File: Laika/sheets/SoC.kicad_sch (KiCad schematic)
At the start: 2 parts, among them J6 Conn_01x03, U1 Milk-V Duo Module

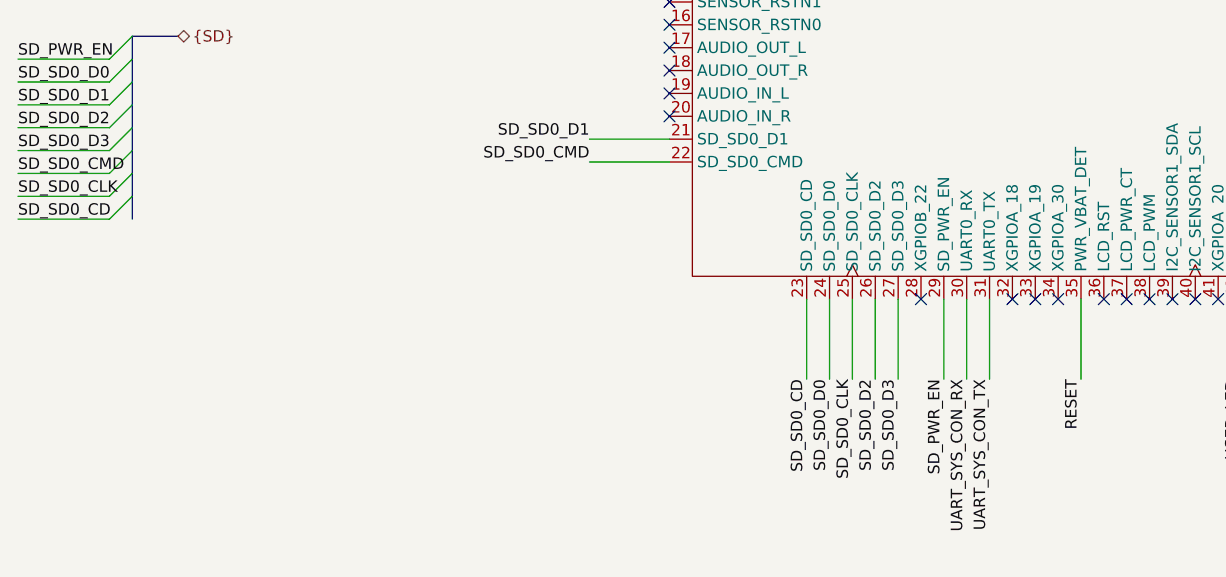
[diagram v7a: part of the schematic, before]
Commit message: Connected LoRa module to UART1 with reset
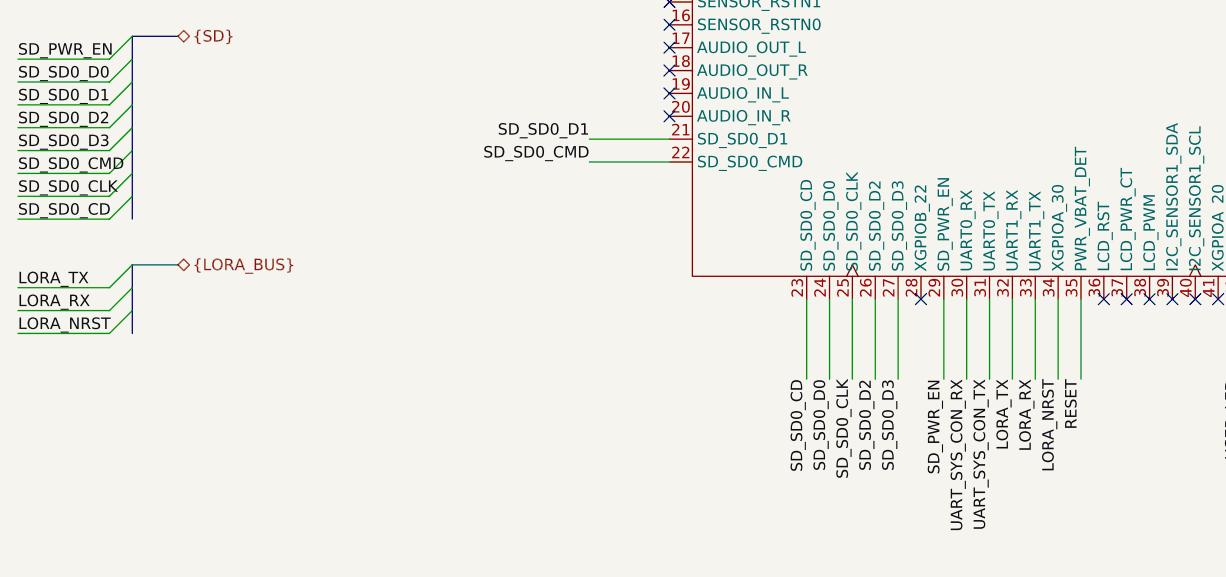
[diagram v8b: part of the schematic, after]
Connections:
- net LORA_TX: now reaches U1.32 (XGPIOA_18)
- net LORA_RX: now reaches U1.33 (XGPIOA_19)
- net LORA_NRST: now reaches U1.34 (XGPIOA_30)
- no-connect marks 66 -> 63
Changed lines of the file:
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@@
-	)
-	(no_connect
-		(at 135.89 143.51)
 	)
 	(no_connect
@@
 	)
 	(no_connect
-		(at 138.43 143.51)
-	)
-	(no_connect
 		(at 97.79 110.49)
 	)
@@
 	(no_connect
 		(at 115.57 59.69)
-	)
-	(no_connect
-		(at 140.97 143.51)
 	)
 	(no_connect
@@
 	)
 	(bus_entry
+		(at 38.1 142.24)
+		(size -2.54 2.54)
+		(stroke
+			(width 0)
+			(type default)
+		)
+	)
+	(bus_entry
+		(at 38.1 139.7)
+		(size -2.54 2.54)
+		(stroke
+			(width 0)
+			(type default)
+		)
+	)
+	(bus_entry
 		(at 38.1 129.54)
 		(size -2.54 2.54)
@@
 	)
 	(bus_entry
+		(at 38.1 144.78)
+		(size -2.54 2.54)
+		(stroke
+			(width 0)
+			(type default)
+		)
+	)
+	(bus_entry
 		(at 38.1 73.66)
 		(size -2.54 2.54)
@@
 	(wire
 		(pts
+			(xy 140.97 152.4) (xy 140.97 143.51)
+		)
+		(stroke
+			(width 0)
+			(type default)
+		)
+	)
+	(wire
+		(pts
 			(xy 113.03 152.4) (xy 113.03 143.51)
 		)
@@
 	(wire
 		(pts
+			(xy 25.4 147.32) (xy 35.56 147.32)
+		)
+		(stroke
+			(width 0)
+			(type default)
+		)
+	)
+	(bus
+		(pts
+			(xy 38.1 139.7) (xy 38.1 142.24)
+		)
+		(stroke
+			(width 0)
+			(type default)
+		)
+	)
+	(wire
+		(pts
 			(xy 143.51 152.4) (xy 143.51 143.51)
 		)
@@
 	(wire
 		(pts
+			(xy 25.4 144.78) (xy 35.56 144.78)
+		)
+		(stroke
+			(width 0)
+			(type default)
+		)
+	)
+	(wire
+		(pts
 			(xy 118.11 143.51) (xy 118.11 152.4)
 		)
@@
 	(bus
 		(pts
+			(xy 38.1 142.24) (xy 38.1 144.78)
+		)
+		(stroke
+			(width 0)
+			(type default)
+		)
+	)
+	(bus
+		(pts
 			(xy 38.1 121.92) (xy 38.1 124.46)
 		)
@@
 		)
 	)
+	(wire
+		(pts
+			(xy 138.43 152.4) (xy 138.43 143.51)
+		)
+		(stroke
+			(width 0)
+			(type default)
+		)
+	)
 	(bus
 		(pts
@@
 		)
 	)
+	(bus
+		(pts
+			(xy 43.18 139.7) (xy 38.1 139.7)
+		)
+		(stroke
+			(width 0)
+			(type default)
+		)
+	)
 	(wire
 		(pts
@@
 	(wire
 		(pts
+			(xy 135.89 152.4) (xy 135.89 143.51)
+		)
+		(stroke
+			(width 0)
+			(type default)
+		)
+	)
+	(wire
+		(pts
 			(xy 166.37 143.51) (xy 185.42 143.51)
 		)
@@
 		)
 	)
+	(wire
+		(pts
+			(xy 25.4 142.24) (xy 35.56 142.24)
+		)
+		(stroke
+			(width 0)
+			(type default)
+		)
+	)
 	(bus
 		(pts
@@
 		(pts
 			(xy 38.1 73.66) (xy 38.1 76.2)
+		)
+		(stroke
+			(width 0)
+			(type default)
+		)
+	)
+	(bus
+		(pts
+			(xy 38.1 144.78) (xy 38.1 147.32)
 		)
 		(stroke
@@
 		)
 	)
+	(label "LORA_RX"
+		(at 25.4 144.78 0)
+		(effects
+			(font
+				(size 1.27 1.27)
+			)
+			(justify left bottom)
+		)
+	)
 	(label "AARCH_SEL"
 		(at 25.4 96.52 0)
@@
 		)
 	)
+	(label "LORA_RX"
+		(at 138.43 152.4 270)
+		(effects
+			(font
+				(size 1.27 1.27)
+			)
+			(justify right bottom)
+		)
+	)
+	(label "LORA_TX"
+		(at 25.4 142.24 0)
+		(effects
+			(font
+				(size 1.27 1.27)
+			)
+			(justify left bottom)
+		)
+	)
 	(label "USB_DM"
 		(at 25.4 73.66 0)
@@
 		)
 	)
+	(label "LORA_NRST"
+		(at 140.97 152.4 270)
+		(effects
+			(font
+				(size 1.27 1.27)
+			)
+			(justify right bottom)
+		)
+	)
 	(label "RESET"
 		(at 143.51 152.4 270)
@@
 		)
 	)
+	(label "LORA_TX"
+		(at 135.89 152.4 270)
+		(effects
+			(font
+				(size 1.27 1.27)
+			)
+			(justify right bottom)
+		)
+	)
 	(label "SD_SD0_D2"
 		(at 25.4 124.46 0)
@@
 		)
 	)
+	(label "LORA_NRST"
+		(at 25.4 147.32 0)
+		(effects
+			(font
+				(size 1.27 1.27)
+			)
+			(justify left bottom)
+		)
+	)
 	(label "UART_SYS_CON_TX"
 		(at 133.35 152.4 270)
@@
 			)
 			(justify right bottom)
+		)
+	)
+	(hierarchical_label "{LORA_BUS}"
+		(shape bidirectional)
+		(at 43.18 139.7 0)
+		(effects
+			(font
+				(size 1.27 1.27)
+			)
+			(justify left)
 		)
 	)
@@
 		)
 		(pin "32"
+			(alternate "UART1_RX")
 		)
 		(pin "49"
@@
 		)
 		(pin "33"
+			(alternate "UART1_TX")
 		)
 		(pin "68"
